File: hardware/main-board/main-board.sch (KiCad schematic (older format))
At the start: 78 parts, among them J1 USB_B_Micro, J2 STDC14, J3 Display Connector, J4 Conn_01x02, SW1 SW_Push, SW2 SW_Push, SW3 SW_Push, SW4 SW_Push, SW5 SW_Detect, U1 TSL2591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

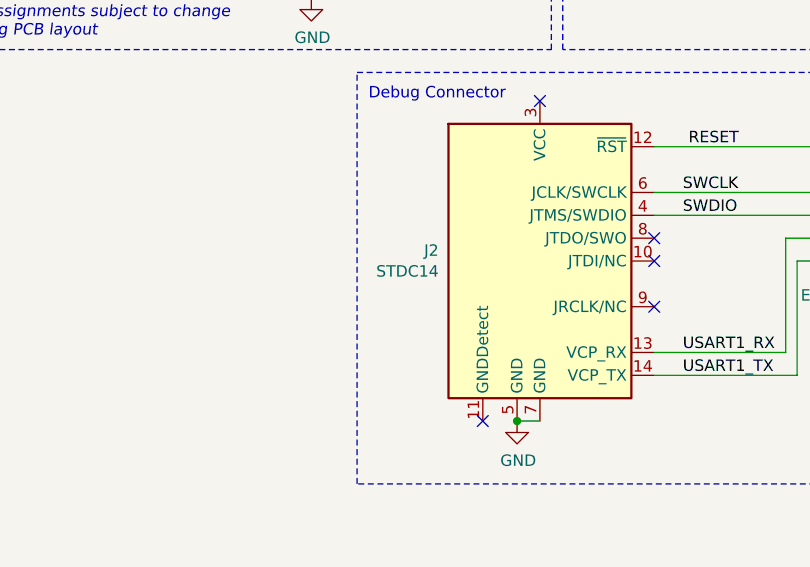
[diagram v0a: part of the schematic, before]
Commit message: Switched debug connector to a Tag-Connect TC2070
This makes it easier to put on the opposite side of the board, where it
won't be obstructed.
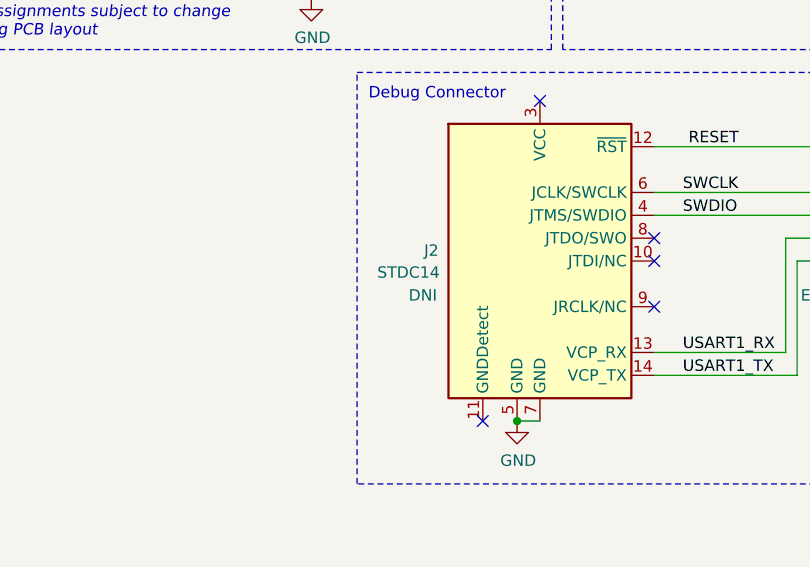
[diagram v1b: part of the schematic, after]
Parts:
- J2: value STDC14 -> DNI; footprint lib_fp:Samtec_FTSH-107-01-L-DV-K-A_2x07_P1.27mm -> Connector:Tag-Connect_TC2070-IDC-FP_2x07_P1.27mm_Vertical; Description CONN HEADER SMD 14POS 1.27MM -> (none); Manufacturer Samtec Inc. -> Tag-Connect; Manufacturer PN FTSH-107-01-L-DV-K-A -> TC2070-IDC-050; Supplier Mouser -> (none); Supplier PN 200-FTSH10701LDVKA -> (none); User Label (none) -> STDC14
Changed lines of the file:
@@
 	6025 5050 6650 5050
 Wire Wire Line
-	6650 4550 6725 4550
-Wire Wire Line
-	6650 5050 6650 4550
-Wire Wire Line
 	6025 4950 6600 4950
-Wire Wire Line
-	6600 4450 6725 4450
-Wire Wire Line
-	6600 4950 6600 4450
 Wire Wire Line
 	6025 4350 6725 4350
@@
 P 5525 4550
 F 0 "J2" H 5082 4596 50  0000 R CNN
-F 1 "STDC14" H 5082 4505 50  0000 R CNN
-F 2 "lib_fp:Samtec_FTSH-107-01-L-DV-K-A_2x07_P1.27mm" H 5525 3450 50  0001 C CNN
-F 3 "https://www.mouser.com/datasheet/2/527/ftsh_smt-1316912.pdf" V 5175 3300 50  0001 C CNN
-F 4 "CONN HEADER SMD 14POS 1.27MM" H 5525 4550 50  0001 C CNN "Description"
-F 5 "Samtec Inc." H 5525 4550 50  0001 C CNN "Manufacturer"
-F 6 "FTSH-107-01-L-DV-K-A" H 5525 4550 50  0001 C CNN "Manufacturer PN"
-F 7 "Mouser" H 5525 4550 50  0001 C CNN "Supplier"
-F 8 "200-FTSH10701LDVKA" H 5525 4550 50  0001 C CNN "Supplier PN"
+F 1 "DNI" H 5075 4400 50  0000 R CNN
+F 2 "Connector:Tag-Connect_TC2070-IDC-FP_2x07_P1.27mm_Vertical" H 5525 3450 50  0001 C CNN
+F 3 "https://www.tag-connect.com/wp-content/uploads/bsk-pdf-manager/TC2070-IDC_Datasheet_11.pdf" V 5175 3300 50  0001 C CNN
+F 4 "Tag-Connect" H 5525 4550 50  0001 C CNN "Manufacturer"
+F 5 "TC2070-IDC-050" H 5525 4550 50  0001 C CNN "Manufacturer PN"
+F 6 "STDC14" H 4950 4500 50  0000 C CNN "User Label"
 	1    5525 4550
 	1    0    0    -1
@@
 Wire Wire Line
 	1125 6975 1525 6975
+Wire Wire Line
+	6650 5050 6650 4550
+Wire Wire Line
+	6650 4550 6725 4550
+Wire Wire Line
+	6600 4950 6600 4450
+Wire Wire Line
+	6600 4450 6725 4450
 $EndSCHEMATC

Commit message: Net tie cleanup
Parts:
- NT1: footprint NetTie:NetTie-2_SMD_Pad0.5mm -> lib_fp:NetTie-2_SMD_Pad_20mil
- NT2: footprint NetTie:NetTie-2_SMD_Pad0.5mm -> lib_fp:NetTie-2_SMD_Pad_10mil
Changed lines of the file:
@@
 F 0 "NT1" H 1825 4300 50  0000 C CNN
 F 1 "Net-Tie_2" H 1825 4440 50  0001 C CNN
-F 2 "NetTie:NetTie-2_SMD_Pad0.5mm" H 1825 4350 50  0001 C CNN
+F 2 "lib_fp:NetTie-2_SMD_Pad_20mil" H 1825 4350 50  0001 C CNN
 F 3 "~" H 1825 4350 50  0001 C CNN
 	1    1825 4350
@@
 F 0 "NT2" H 7500 2325 50  0000 C CNN
 F 1 "Net-Tie_2" H 7500 2365 50  0001 C CNN
-F 2 "NetTie:NetTie-2_SMD_Pad0.5mm" H 7500 2275 50  0001 C CNN
+F 2 "lib_fp:NetTie-2_SMD_Pad_10mil" H 7500 2275 50  0001 C CNN
 F 3 "~" H 7500 2275 50  0001 C CNN
 	1    7500 2275

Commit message: Test point cleanup
We don't have clearance for test point attachments on top of the PCB.
Instead, the rear screw holes will be connected to ground, and 5V for
testing will just be supplied via the USB connector like normal power.
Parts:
- removed TP1: 5V, TestPoint:TestPoint_Keystone_5005-5009_Compact, symbol Connector:TestPoint
- removed TP3: GND, TestPoint:TestPoint_Keystone_5005-5009_Compact, symbol Connector:TestPoint
- H5, H6: footprint MountingHole:MountingHole_2.2mm_M2 -> MountingHole:MountingHole_2.2mm_M2_Pad_Via; symbol Mechanical:MountingHole -> Mechanical:MountingHole_Pad
- renumbered TP2 to TP1
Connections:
- net GND: now also H5.1, H6.1
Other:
- moved on the sheet: H1, H2, H3, H4
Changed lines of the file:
@@
 L Mechanical:MountingHole H1
 U 1 1 60572EAB
-P 9700 5400
-F 0 "H1" H 9800 5446 50  0000 L CNN
-F 1 "MountingHole" H 9800 5355 50  0000 L CNN
-F 2 "MountingHole:MountingHole_2.2mm_M2" H 9700 5400 50  0001 C CNN
-F 3 "~" H 9700 5400 50  0001 C CNN
-	1    9700 5400
+P 8850 5400
+F 0 "H1" H 8950 5446 50  0000 L CNN
+F 1 "MountingHole" H 8950 5355 50  0000 L CNN
+F 2 "MountingHole:MountingHole_2.2mm_M2" H 8850 5400 50  0001 C CNN
+F 3 "~" H 8850 5400 50  0001 C CNN
+	1    8850 5400
 	1    0    0    -1
 $EndComp
@@
 L Mechanical:MountingHole H2
 U 1 1 60573343
-P 9700 5625
-F 0 "H2" H 9800 5671 50  0000 L CNN
-F 1 "MountingHole" H 9800 5580 50  0000 L CNN
-F 2 "MountingHole:MountingHole_2.2mm_M2" H 9700 5625 50  0001 C CNN
-F 3 "~" H 9700 5625 50  0001 C CNN
-	1    9700 5625
+P 8850 5625
+F 0 "H2" H 8950 5671 50  0000 L CNN
+F 1 "MountingHole" H 8950 5580 50  0000 L CNN
+F 2 "MountingHole:MountingHole_2.2mm_M2" H 8850 5625 50  0001 C CNN
+F 3 "~" H 8850 5625 50  0001 C CNN
+	1    8850 5625
 	1    0    0    -1
 $EndComp
@@
 L Mechanical:MountingHole H3
 U 1 1 605736BA
-P 9700 5850
-F 0 "H3" H 9800 5896 50  0000 L CNN
-F 1 "MountingHole" H 9800 5805 50  0000 L CNN
-F 2 "MountingHole:MountingHole_2.2mm_M2" H 9700 5850 50  0001 C CNN
-F 3 "~" H 9700 5850 50  0001 C CNN
-	1    9700 5850
+P 8850 5850
+F 0 "H3" H 8950 5896 50  0000 L CNN
+F 1 "MountingHole" H 8950 5805 50  0000 L CNN
+F 2 "MountingHole:MountingHole_2.2mm_M2" H 8850 5850 50  0001 C CNN
+F 3 "~" H 8850 5850 50  0001 C CNN
+	1    8850 5850
 	1    0    0    -1
 $EndComp
@@
 L Mechanical:MountingHole H4
 U 1 1 605739B5
-P 9700 6075
-F 0 "H4" H 9800 6121 50  0000 L CNN
-F 1 "MountingHole" H 9800 6030 50  0000 L CNN
-F 2 "MountingHole:MountingHole_2.2mm_M2" H 9700 6075 50  0001 C CNN
-F 3 "~" H 9700 6075 50  0001 C CNN
-	1    9700 6075
-	1    0    0    -1
-$EndComp
-$Comp
-L Mechanical:MountingHole H5
+P 8850 6075
+F 0 "H4" H 8950 6121 50  0000 L CNN
+F 1 "MountingHole" H 8950 6030 50  0000 L CNN
+F 2 "MountingHole:MountingHole_2.2mm_M2" H 8850 6075 50  0001 C CNN
+F 3 "~" H 8850 6075 50  0001 C CNN
+	1    8850 6075
+	1    0    0    -1
+$EndComp
+$Comp
+L Mechanical:MountingHole_Pad H5
 U 1 1 60573BE2
-P 9700 6300
-F 0 "H5" H 9800 6346 50  0000 L CNN
-F 1 "MountingHole" H 9800 6255 50  0000 L CNN
-F 2 "MountingHole:MountingHole_2.2mm_M2" H 9700 6300 50  0001 C CNN
-F 3 "~" H 9700 6300 50  0001 C CNN
-	1    9700 6300
-	1    0    0    -1
-$EndComp
-$Comp
-L Mechanical:MountingHole H6
+P 9650 5450
+F 0 "H5" H 9750 5550 50  0000 L CNN
+F 1 "MountingHole" H 9750 5450 50  0000 L CNN
+F 2 "MountingHole:MountingHole_2.2mm_M2_Pad_Via" H 9650 5450 50  0001 C CNN
+F 3 "~" H 9650 5450 50  0001 C CNN
+	1    9650 5450
+	1    0    0    -1
+$EndComp
+$Comp
+L Mechanical:MountingHole_Pad H6
 U 1 1 60573EB9
-P 9700 6525
-F 0 "H6" H 9800 6571 50  0000 L CNN
-F 1 "MountingHole" H 9800 6480 50  0000 L CNN
-F 2 "MountingHole:MountingHole_2.2mm_M2" H 9700 6525 50  0001 C CNN
-F 3 "~" H 9700 6525 50  0001 C CNN
-	1    9700 6525
+P 9650 5900
+F 0 "H6" H 9750 6000 50  0000 L CNN
+F 1 "MountingHole" H 9750 5900 50  0000 L CNN
+F 2 "MountingHole:MountingHole_2.2mm_M2_Pad_Via" H 9650 5900 50  0001 C CNN
+F 3 "~" H 9650 5900 50  0001 C CNN
+	1    9650 5900
 	1    0    0    -1
 $EndComp
@@
 	10125 2175 10125 2075
 Connection ~ 9325 2175
-$Comp
-L Connector:TestPoint TP1
-U 1 1 6066F1AB
-P 3875 6625
-F 0 "TP1" H 3800 6850 50  0000 L CNN
-F 1 "5V" H 3933 6652 50  0001 L CNN
-F 2 "TestPoint:TestPoint_Keystone_5005-5009_Compact" H 4075 6625 50  0001 C CNN
-F 3 "http://www.keyelco.com/product-pdf.cfm?p=1314" H 4075 6625 50  0001 C CNN
-F 4 "PC TEST POINT COMPACT BLACK" H 3875 6625 50  0001 C CNN "Description"
-F 5 "Keystone Electronics" H 3875 6625 50  0001 C CNN "Manufacturer"
-F 6 "5006" H 3875 6625 50  0001 C CNN "Manufacturer PN"
-F 7 "Digi-Key" H 3875 6625 50  0001 C CNN "Supplier"
-F 8 "36-5006-ND" H 3875 6625 50  0001 C CNN "Supplier PN"
-	1    3875 6625
-	-1   0    0    1
-$EndComp
 NoConn ~ 725  7575
 NoConn ~ 1750 1525
@@
 Wire Notes Line
 	2950 3625 5575 3625
-Wire Wire Line
-	825  7575 1100 7575
-Connection ~ 825  7575
-$Comp
-L Connector:TestPoint TP3
-U 1 1 605B26C3
-P 1100 7575
-F 0 "TP3" H 1025 7800 50  0000 L CNN
-F 1 "GND" H 1158 7602 50  0001 L CNN
-F 2 "TestPoint:TestPoint_Keystone_5005-5009_Compact" H 1300 7575 50  0001 C CNN
-F 3 "http://www.keyelco.com/product-pdf.cfm?p=1314" H 1300 7575 50  0001 C CNN
-F 4 "PC TEST POINT COMPACT BLACK" H 1100 7575 50  0001 C CNN "Description"
-F 5 "Keystone Electronics" H 1100 7575 50  0001 C CNN "Manufacturer"
-F 6 "5006" H 1100 7575 50  0001 C CNN "Manufacturer PN"
-F 7 "Digi-Key" H 1100 7575 50  0001 C CNN "Supplier"
-F 8 "36-5006-ND" H 1100 7575 50  0001 C CNN "Supplier PN"
-	1    1100 7575
-	-1   0    0    1
-$EndComp
 Text Label 1125 7175 0    50   ~ 0
 USB_CONN_D+
@@
 Connection ~ 2000 5550
 $Comp
-L Connector:TestPoint TP2
+L Connector:TestPoint TP1
 U 1 1 60670A35
 P 2000 5550
-F 0 "TP2" H 2058 5622 50  0000 L CNN
+F 0 "TP1" H 2058 5622 50  0000 L CNN
 F 1 "3.3V" H 2058 5577 50  0001 L CNN
 F 2 "TestPoint:TestPoint_Pad_D2.0mm" H 2200 5550 50  0001 C CNN
@@
 Wire Wire Line
 	6600 4450 6725 4450
+$Comp
+L power:GND #PWR0124
+U 1 1 60CBE3DA
+P 9650 5550
+F 0 "#PWR0124" H 9650 5300 50  0001 C CNN
+F 1 "GND" H 9650 5400 50  0000 C CNN
+F 2 "" H 9650 5550 50  0001 C CNN
+F 3 "" H 9650 5550 50  0001 C CNN
+	1    9650 5550
+	1    0    0    -1
+$EndComp
+$Comp
+L power:GND #PWR0132
+U 1 1 60CBE6B6
+P 9650 6000
+F 0 "#PWR0132" H 9650 5750 50  0001 C CNN
+F 1 "GND" H 9650 5850 50  0000 C CNN
+F 2 "" H 9650 6000 50  0001 C CNN
+F 3 "" H 9650 6000 50  0001 C CNN
+	1    9650 6000
+	1    0    0    -1
+$EndComp
 $EndSCHEMATC

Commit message: Change MCU component value to 64KB flash variant
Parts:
- U2: value STM32L052K6U6 -> STM32L052K8U6; symbol MCU_ST_STM32L0:STM32L052K6Ux -> MCU_ST_STM32L0:STM32L052K8Ux; Description IC MCU 32BIT 32KB FLASH 32UFQFPN -> IC MCU 32BIT 64KB FLASH 32UFQFPN; Manufacturer PN STM32L052K6U6 -> STM32L052K8U6; Supplier PN 497-17492-ND -> 497-17494-ND
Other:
- note removed: "Pin assignments subject to change\nduring PCB layout"
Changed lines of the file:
@@
 $EndDescr
 $Comp
-L MCU_ST_STM32L0:STM32L052K6Ux U2
+L MCU_ST_STM32L0:STM32L052K8Ux U2
 U 1 1 6056A21B
 P 4525 2400
 F 0 "U2" H 4100 3250 50  0000 C CNN
-F 1 "STM32L052K6U6" H 4900 1450 50  0000 C CNN
+F 1 "STM32L052K8U6" H 4900 1450 50  0000 C CNN
 F 2 "lib_fp:ST_UFQFPN32" H 4025 1500 50  0001 R CNN
 F 3 "http://www.st.com/st-web-ui/static/active/en/resource/technical/document/datasheet/DM00108217.pdf" H 4525 2400 50  0001 C CNN
-F 4 "IC MCU 32BIT 32KB FLASH 32UFQFPN" H 4525 2400 50  0001 C CNN "Description"
+F 4 "IC MCU 32BIT 64KB FLASH 32UFQFPN" H 4525 2400 50  0001 C CNN "Description"
 F 5 "STMicroelectronics" H 4525 2400 50  0001 C CNN "Manufacturer"
-F 6 "STM32L052K6U6" H 4525 2400 50  0001 C CNN "Manufacturer PN"
+F 6 "STM32L052K8U6" H 4525 2400 50  0001 C CNN "Manufacturer PN"
 F 7 "Digi-Key" H 4525 2400 50  0001 C CNN "Supplier"
-F 8 "497-17492-ND" H 4525 2400 50  0001 C CNN "Supplier PN"
+F 8 "497-17494-ND" H 4525 2400 50  0001 C CNN "Supplier PN"
 	1    4525 2400
 	1    0    0    -1
@@
 Wire Wire Line
 	5025 2500 5475 2500
-Text Notes 2975 3575 0    50   Italic 0
-Pin assignments subject to change\nduring PCB layout
 Wire Wire Line
 	7800 1275 7800 1375

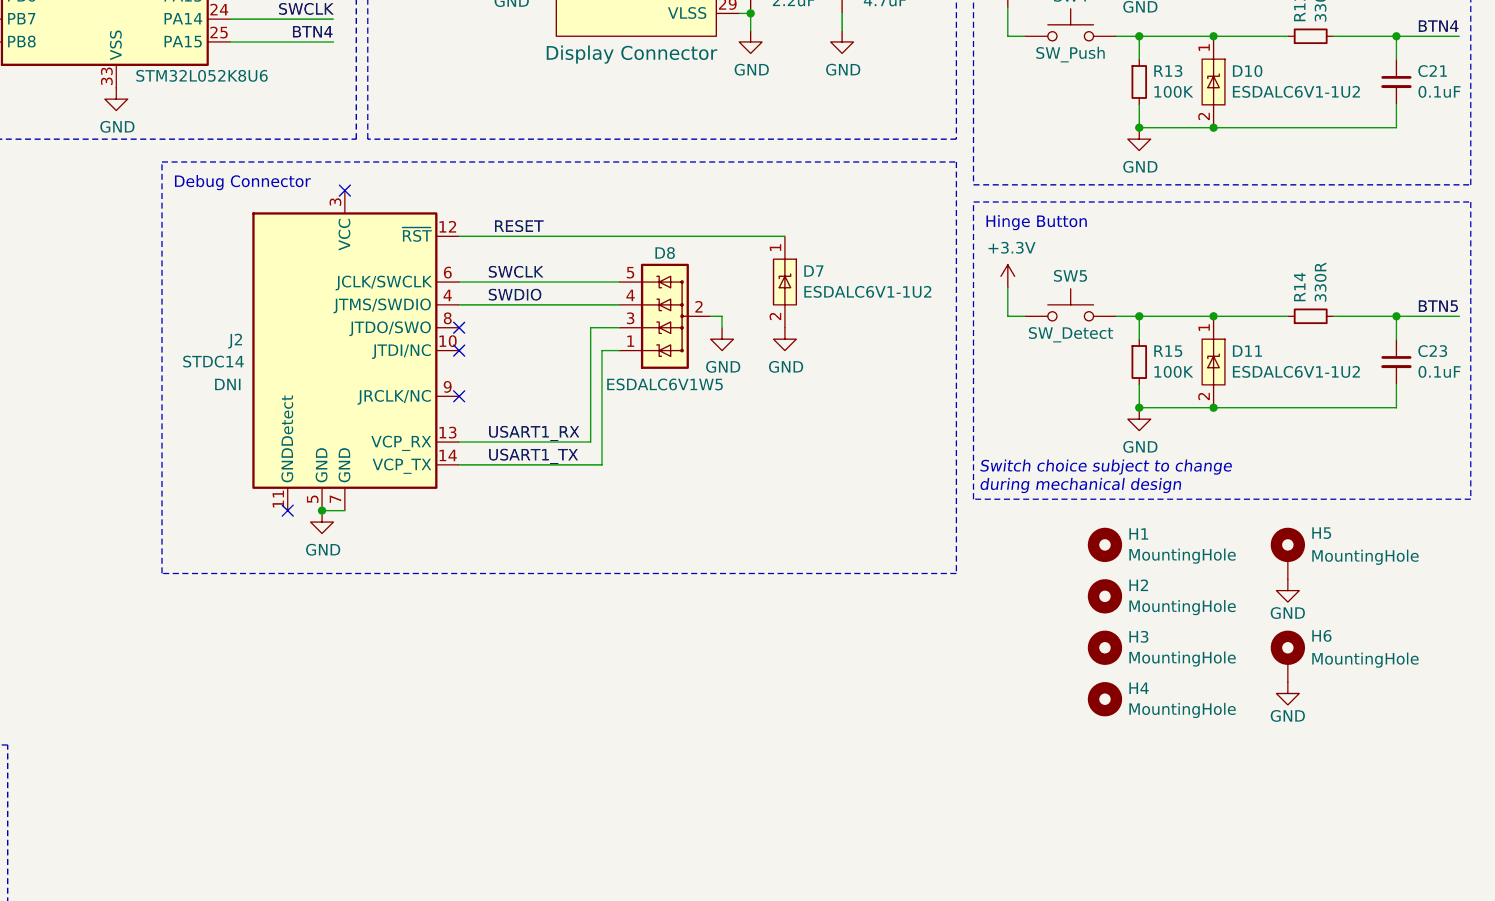
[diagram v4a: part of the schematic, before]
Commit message: Connect power to debug connector
This allows the ST-Link to detect the target voltage, but otherwise
isn't really necessary. Still probably a good idea to have, though.
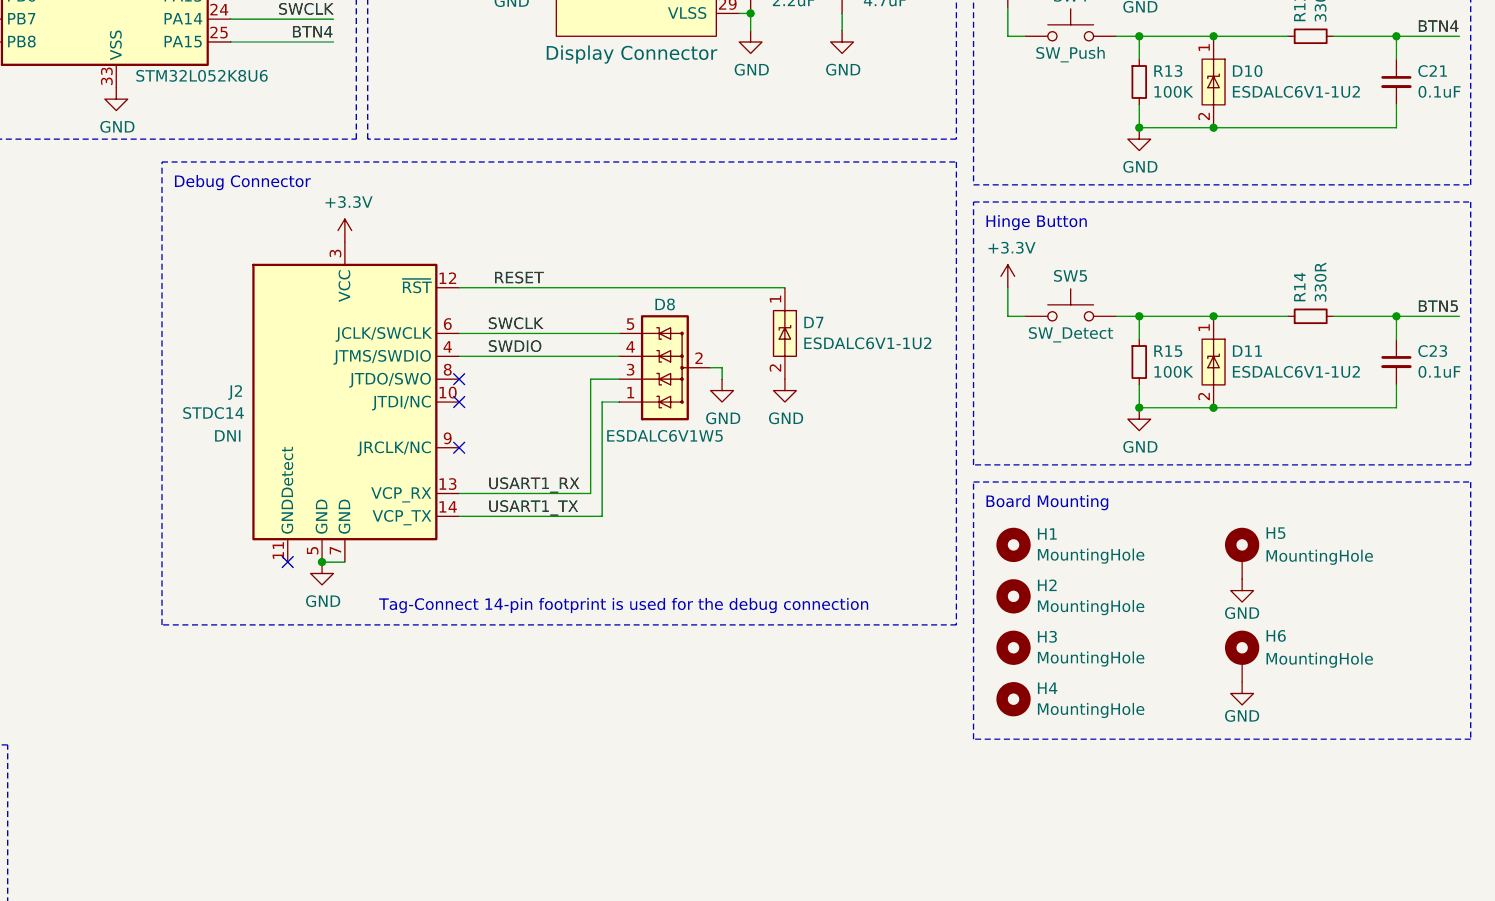
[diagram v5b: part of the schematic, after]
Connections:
- net +3V3: now also J2.3 (VCC)
- no-connect marks 18 -> 17
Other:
- note added: "Board Mounting"
- note added: "Tag-Connect 14-pin footprint is used for the debug connection"
- note removed: "Switch choice subject to change\nduring mechanical design"
- moved on the sheet: D7, D8, H1, H2, H3, H4, H5, H6, J2
